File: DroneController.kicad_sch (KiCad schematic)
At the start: 57 parts, among them J1 Connector, J2 Connector, J3 Connector, J4 UART Flash, J5 UART Flash, P1 USB_C_Plug, Q2 AO3400A, Q3 AO3400A, SW2 SW_SPDT, U2 W25Q16JVSS, U3 BMP280, U4 MPU-6500, U6 L86-M33, U7 915MHz, U9 AP7361C-33E, X1 Shenzhen SCTF Elec SX2B12.000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

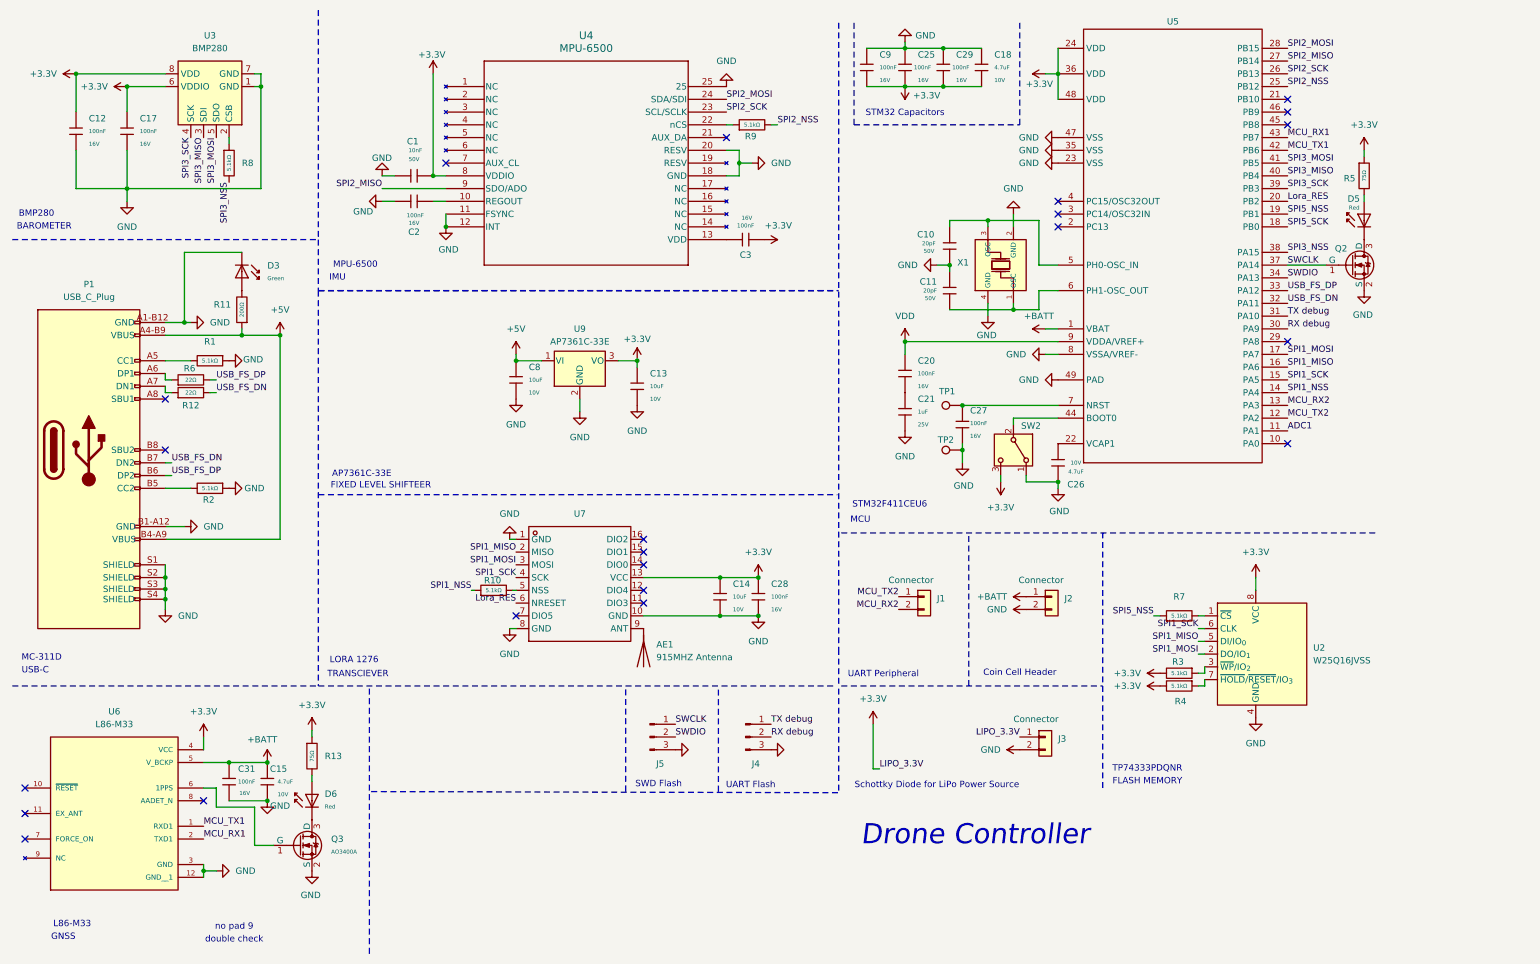
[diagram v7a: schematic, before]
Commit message: Fixed wiring, Added pull-up on CS, respecced IMU, began work on a new layout
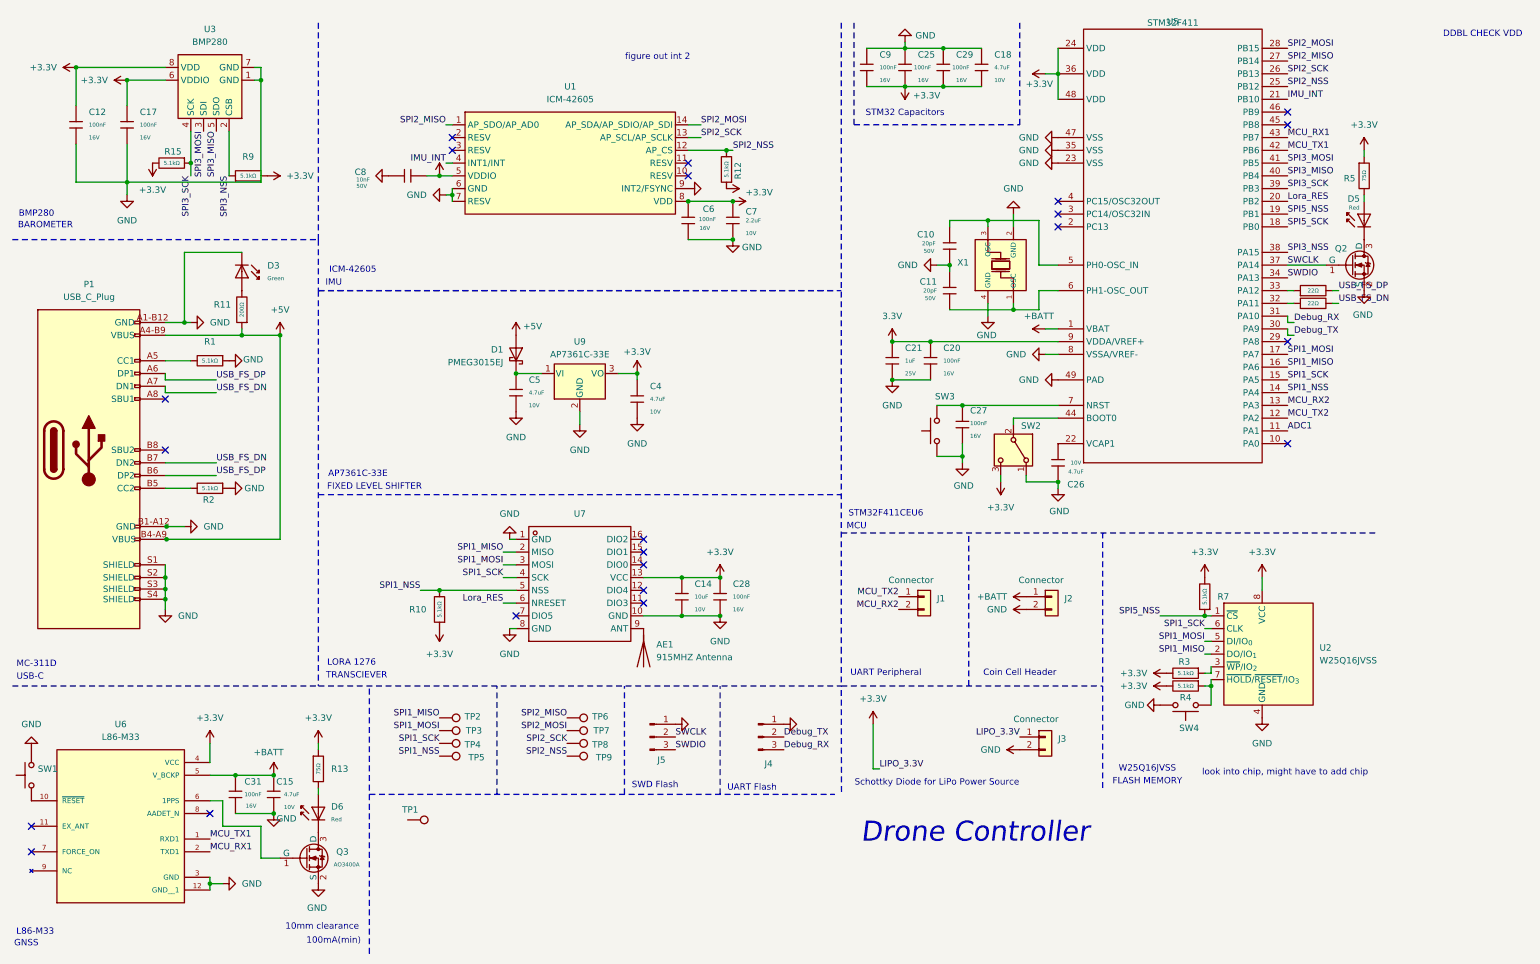
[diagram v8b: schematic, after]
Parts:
- removed C1: 10nF, PCM_JLCPCB:C_0402, symbol PCM_JLCPCB-Capacitors:0402,10nF
- removed C13, C8: 10uF, PCM_JLCPCB:C_0402, symbol PCM_JLCPCB-Capacitors:0402,10uF
- removed C2, C3: 100nF, PCM_JLCPCB:C_0402, symbol PCM_JLCPCB-Capacitors:0402,100nF
- removed R12: 22Ω, PCM_JLCPCB:R_0402, symbol PCM_JLCPCB-Resistors:0402,22Ω
- removed R8: 5.1kΩ, PCM_JLCPCB:R_0402, symbol PCM_JLCPCB-Resistors:0402,5.1kΩ
- removed U4: MPU-6500, QFN24_3X3X0P9_IVS, symbol MPU-6500:MPU-6500
- added C4, C5: 4.7uF, PCM_JLCPCB:C_0402, symbol PCM_JLCPCB-Capacitors:0402,4.7uF
- added C6: 100nF, PCM_JLCPCB:C_0402, symbol PCM_JLCPCB-Capacitors:0402,100nF
- added C7: 2.2uF, PCM_JLCPCB:C_0402, symbol PCM_JLCPCB-Capacitors:0402,2.2uF
- added C8: 10nF, PCM_JLCPCB:C_0402, symbol PCM_JLCPCB-Capacitors:0402,10nF
- added D1: PMEG3015EJ, Diode_SMD:D_SOD-323F, symbol Diode:PMEG3015EJ
- added R12, R15: 5.1kΩ, PCM_JLCPCB:R_0402, symbol PCM_JLCPCB-Resistors:0402,5.1kΩ
- added R14: 22Ω, PCM_JLCPCB:R_0402, symbol PCM_JLCPCB-Resistors:0402,22Ω
- added SW1, SW3, SW4: SW_Push, symbol Switch:SW_Push
- added TP3, TP4, TP5, TP6, TP7, TP8, TP9: TestPoint, TestPoint:TestPoint_Keystone_5019_Miniature, symbol Connector:TestPoint
- added U1: ICM-42605, easyeda2kicad:LGA-14_L3.0-W2.5-P0.50-TL, symbol easyeda2kicad:ICM-42605
- TP1: footprint (none) -> TestPoint:TestPoint_Pad_1.0x1.0mm
- TP2: footprint (none) -> TestPoint:TestPoint_Keystone_5019_Miniature
- U5: value ~ -> STM32F411
- U6: Manufacturer Product Number  (none) -> L86-M33
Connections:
- net VDD is gone; now on net 3.3V: C20.1, U5.9 (VDDA/VREF+)
- net +3.3V: now also R10.1, R7.2, R9.2, C4.1, C6.2, C7.1, C8.2, R12.1, R15.2, U1.5 (VDDIO), U1.8 (VDD)
- net +5V: now also D1.2 (A); no longer U9.1 (VI)
- net GND: now also C20.2, J4.1 (Pin_1), J5.1 (Pin_1), C4.2, C5.2, C6.1, C7.2, C8.1, SW1.2, SW3.1, SW4.2, U1.6 (GND), U1.7 (RESV), U1.9 (INT2/FSYNC); no longer J4.3 (Pin_3), J5.3 (Pin_3), TP2.1
- net SPI1_MISO: now also TP2.1, U2.2 (DO/IO_{1}); no longer U2.5 (DI/IO_{0})
- net SPI1_MOSI: now also U2.5 (DI/IO_{0}), TP3.1; no longer U2.2 (DO/IO_{1})
- net SPI1_NSS: now also R10.2, U7.5 (NSS), TP5.1; no longer R10.1
- net SPI1_SCK: now also TP4.1
- net SPI2_MISO: now also TP6.1, U1.1 (AP_SDO/AP_AD0)
- net SPI2_MOSI: now also TP7.1, U1.14 (AP_SDA/AP_SDIO/AP_SDI)
- net SPI2_NSS: now also R12.2, TP9.1, U1.12 (AP_CS); no longer R9.2
- net SPI2_SCK: now also TP8.1, U1.13 (AP_SCL/AP_SCLK)
- net SPI3_MISO: now also U3.5 (SDO); no longer U3.3 (SDI)
- net SPI3_MOSI: now also U3.3 (SDI); no longer U3.5 (SDO)
- net SPI3_NSS: now also R9.1, U3.2 (CSB)
- net SPI3_SCK: now also R15.1
- net SPI5_NSS: now also U2.1 (~{CS})
- net SWCLK: now also J5.2 (Pin_2); no longer J5.1 (Pin_1)
- net SWDIO: now also J5.3 (Pin_3); no longer J5.2 (Pin_2)
- net USB_FS_DN: now also P1.A7 (DN1), R6.2; no longer U5.32 (PA11)
- net USB_FS_DP: now also P1.A6 (DP1), R14.2; no longer R6.2, U5.33 (PA12)
- net at R4.1, U2.7 (~{HOLD}/~{RESET}/IO_{3}): now also SW4.1
- net at R6.1: now also U5.32 (PA11); no longer P1.A6 (DP1)
- net IMU_INT: now reaches U5.21 (PB10)
- net IMU_INT: now also U1.4 (INT1/INT)
- net at C27.1, U5.7 (NRST): now also SW3.2; no longer TP1.1
- net at U6.10 (~{RESET}): now also SW1.1
- net 3.3V: now reaches C21.1
- net 3.3V: no longer C20.2
- net RX debug  renamed Debug_TX
- net TX debug  renamed Debug_RX
- net Debug_RX: now also J4.3 (Pin_3); no longer J4.1 (Pin_1)
- new net: C5.1, D1.1 (K), U9.1 (VI)
- new net: R14.1, U5.33 (PA12)
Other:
- note added: "100mA(min)"
- note added: "10mm clearance"
- note added: "DDBL CHECK VDD"
- note added: "FIXED LEVEL SHIFTER"
- note added: "ICM-42605"
- note added: "W25Q16JVSS"
- note added: "figure out int 2"
- note added: "look into chip, might have to add chip"
- note removed: "FIXED LEVEL SHIFTEER"
- note removed: "MPU-6500"
- note removed: "TP74333PDQNR"
- note removed: "double check"
- note removed: "no pad 9"
- moved on the sheet: C12, C14, C15, C17, C20, C21, C28, C31, D6, J4, Q3, R10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
